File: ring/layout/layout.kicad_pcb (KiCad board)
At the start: 2 copper layers, 58 x 6.2 mm, 62 parts, among them U1 ?, U10 ?, U11 ?, U12 ?, U13 ?, U14 ?, U15 ?, U2 ?, U3 ?, U4 ?, U5 ?, U6 ?, U7 ?, U8 ?, U9 ?, Y1 38.4MHz

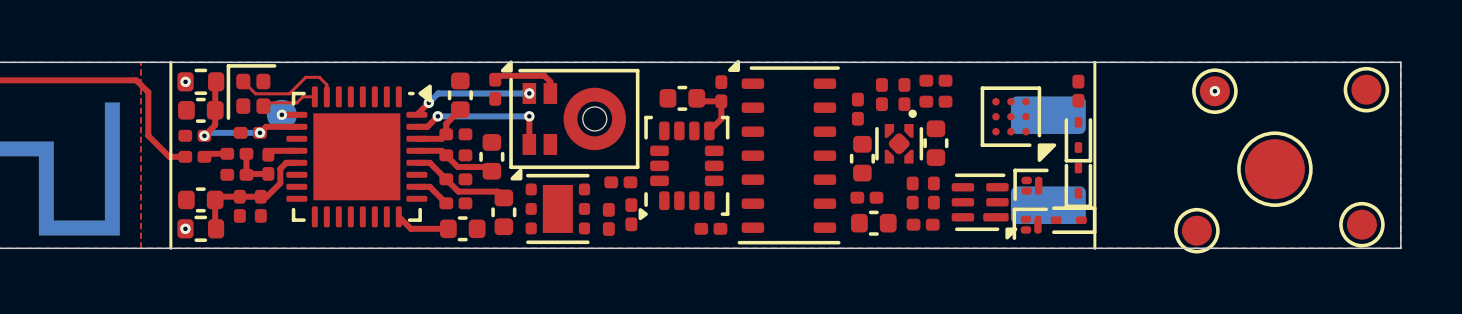
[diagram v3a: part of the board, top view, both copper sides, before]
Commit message: board fully routed; fixing DRC
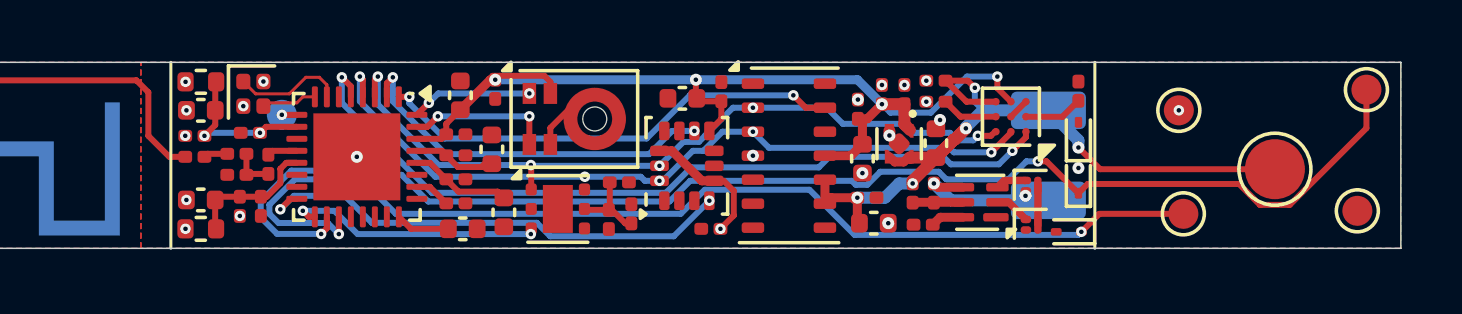
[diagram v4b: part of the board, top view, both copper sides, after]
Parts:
- moved TP6 1.36 mm to (170.6, 81.6)
- moved R2 1.15 mm to (151.9, 84.0), turned to 0 degrees
- moved R1 1.11 mm to (152.3, 85.0), turned to 90 degrees
- moved TP3 0.72 mm to (170.8, 85.0)
- moved TP5 0.49 mm to (176.6, 85.0)
- moved U12 0.39 mm to (166.9, 85.7)
- moved C8 0.25 mm to (147.7, 82.9)
- moved U2 0.16 mm to (166.3, 83.1)
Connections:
- net battery.N59 renamed battery.N61
- net hbt.N152 renamed hbt.N154
- net imu.N232 renamed imu.N234
- net imu.N233 renamed imu.N235
- TP3 pad 1: sda -> swdio
- TP4 pad 1: scl -> swclk
- U12 pad 1: sda -> swdio
- U13 pad 1: scl -> swclk
- U6 pad 1: bat_low -> hbt_int
- U6 pad 14: N381 -> N383
- U6 pad 15: N380 -> N382
- U6 pad 18: N382 -> swclk
- U6 pad 19: N383 -> swdio
- U6 pad 2: hbt_int -> imu_int2
- U6 pad 3: imu_int2 -> scl
- U6 pad 5: scl -> bat_low
- U6 pad 6: N379 -> N381
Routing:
- net swclk: track 0.00 -> 45.2 mm, vias 0 -> 2
- net swdio: track 0.00 -> 36.0 mm, vias 0 -> 2
- net VDD: track 13.8 -> 46.9 mm, vias 2 -> 7
- net bat_low: track 0.00 -> 26.8 mm, vias 0 -> 2
- net VBATT: track 0.00 -> 26.0 mm, vias 0 -> 5
- net sda: track 0.00 -> 25.6 mm, vias 0 -> 5
- net scl: track 0.00 -> 25.3 mm, vias 0 -> 5
- net imu_int1: track 0.00 -> 16.2 mm, vias 0 -> 2
- net hbt_int: track 0.00 -> 15.7 mm, vias 0 -> 2
- net imu_int2: track 0.00 -> 12.6 mm, vias 0 -> 2
- net tmp_int: track 0.00 -> 8.40 mm, vias 0 -> 2
- net battery.bat_vss: track 0.00 -> 5.24 mm, vias 0 -> 2
- net GND: track 0.00 -> 3.35 mm, vias 1 -> 19
- net batman.bin: track 0.00 -> 1.97 mm
- net batman.batman_vdd_out: track 0.00 -> 1.89 mm
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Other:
- rule pad_to_mask_clearance: 0.1 -> 0

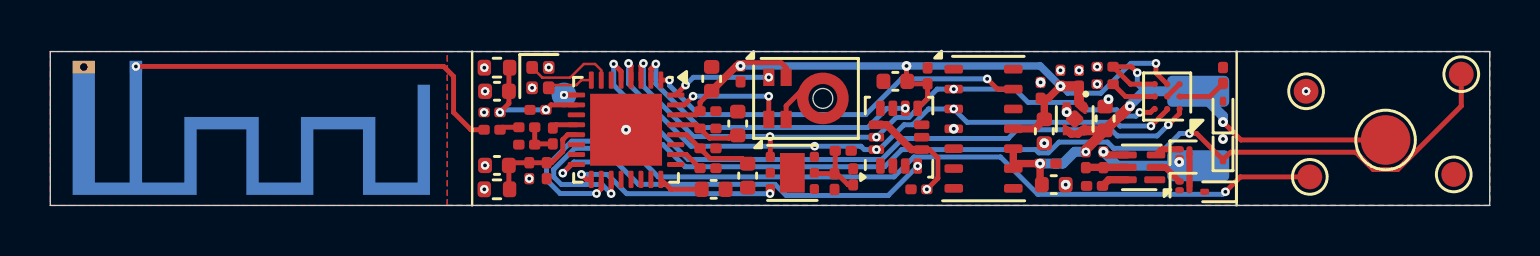
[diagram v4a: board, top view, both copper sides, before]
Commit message: pretty rounded tracks; breaks everything though
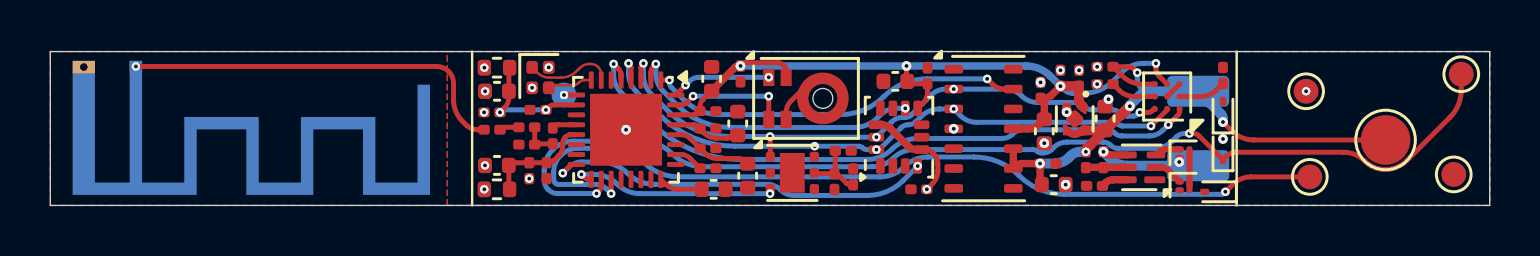
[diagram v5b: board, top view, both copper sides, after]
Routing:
- net VDD: track 46.9 -> 46.0 mm
- net bat_low: track 26.8 -> 26.2 mm
- net VBATT: track 26.0 -> 25.4 mm
- net scl: track 25.3 -> 24.8 mm

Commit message: drc passes
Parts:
- moved TP5 4.26 mm to (180.8, 85.2)
- moved TP6 4.24 mm to (174.8, 81.0)
- moved TP3 4.05 mm to (174.8, 85.2)
- moved TP2 4.02 mm to (177.8, 83.1)
- moved TP4 3.95 mm to (180.8, 81.0)
- moved C6 0.86 mm to (147.3, 83.8)
- moved C8 0.38 mm to (147.7, 82.5)
- moved U4 0.21 mm to (165.7, 85.2)
- moved C5 0.10 mm to (148.1, 85.1)
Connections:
- net N381 renamed NC
- net N382 renamed NC_2
- net N383 renamed NC_3
- net N384 renamed NC_4
- net N385 renamed NC_5
- net N386 renamed NC_6
- net N387 renamed NC_7
- net battery.N61 renamed battery.NC
- net cpu.N520 renamed cpu.NC
- net hbt.N154 renamed hbt.NC
- net imu.N234 renamed imu.NC
- net imu.N235 renamed imu.NC_2
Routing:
- net VDD: track 46.0 -> 77.8 mm, vias 7 -> 10
- net swclk: track 44.8 -> 48.0 mm
- net GND: track 3.30 -> 6.02 mm, vias 19 -> 82
- net swdio: track 35.5 -> 38.1 mm
- net VBATT: track 25.4 -> 27.7 mm
- net scl: track 24.8 -> 26.8 mm
- net sda: track 25.2 -> 26.7 mm
- net imu_int1: track 15.9 -> 14.8 mm
- net mic_data: track 4.02 -> 4.67 mm
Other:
- board size 58 x 6.2 mm -> 62 x 6.2 mm
- board text removed: "we get 6.28 * (dist off finger) extra length!"

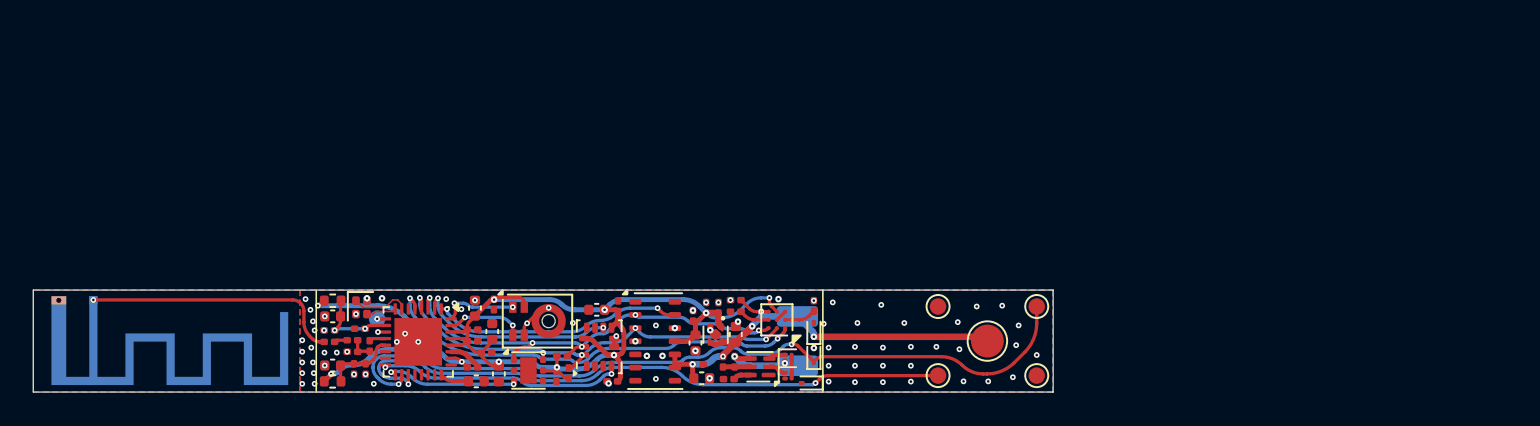
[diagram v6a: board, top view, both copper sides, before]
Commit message: replaced mcu, removed old connections in layout
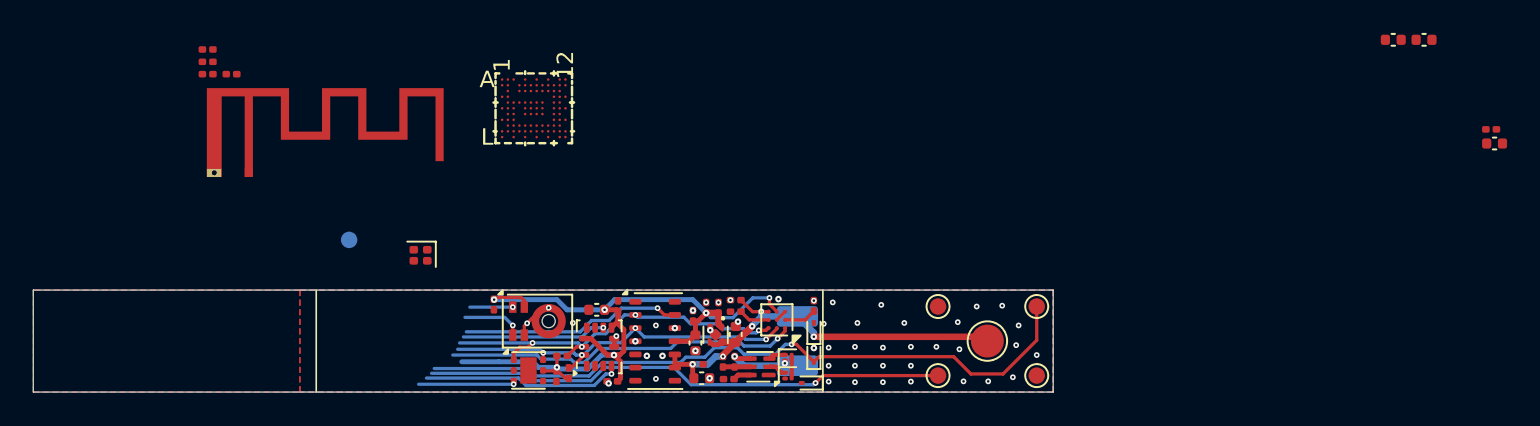
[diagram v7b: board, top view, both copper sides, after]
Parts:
- removed the C10 at (146.7, 81.1)
- removed the C11 at (146.5, 82.4)
- removed the C12 at (139.2, 83.8)
- removed the C13 at (137.8, 83.2)
- removed the C14 at (140.0, 84.8)
- removed the C15 at (139.3, 84.8)
- removed the C16 at (138.0, 84.6)
- removed the C17 at (139.7, 82.3)
- removed the C18 at (137.8, 82.5)
- removed the C19 at (138.0, 81.6)
- removed FB1, FB2: 0 0Hz, R_0402_1005Metric:R_0402_1005Metric
- C5: value 10uF -> 100nF; footprint C_0402_1005Metric:C_0402_1005Metric -> C_0201_0603Metric:C_0201_0603Metric
- C6, C7: value 100nF -> 1uF; footprint C_0201_0603Metric:C_0201_0603Metric -> C_0402_1005Metric:C_0402_1005Metric
- C8: value 1uF -> 1.6pF; footprint C_0402_1005Metric:C_0402_1005Metric -> C_0201_0603Metric:C_0201_0603Metric
- C9: value 10nF -> 18pF
- L2: value 3.2nH -> 3.200000000000001nH
- U6: footprint QFN-32-1EP_4x4mm_P0.4mm_EP2.9x2.9mm:QFN-32-1EP_4x4mm_P0.4mm_EP2.9x2.9mm -> WLCSP95_4.390X3.994_NOR:WLCSP95_4.390X3.994_NOR
- U7: moved to F.Cu
- Y1: value 38.4MHz -> 32MHz; footprint Crystal_SMD_1210-4Pin_1.2x1.0mm:Crystal_SMD_1210-4Pin_1.2x1.0mm -> Crystal_SMD_2016-4Pin_2.0x1.6mm:Crystal_SMD_2016-4Pin_2.0x1.6mm
- moved C6 62.6 mm to (208.6, 71.1)
- moved C5 62.1 mm to (208.4, 70.2), turned to 0 degrees
- moved C7 61.2 mm to (204.3, 64.8)
- moved C4 59.5 mm to (202.5, 64.8)
- moved C9 23.4 mm to (130.4, 66.1)
- moved C8 23.3 mm to (130.4, 66.9), turned to 0 degrees
- moved L2 19.7 mm to (130.4, 65.4), turned to 0 degrees
- moved L1 18.5 mm to (131.8, 66.9), turned to 0 degrees
- moved U6 15.8 mm to (150.2, 69.0), turned to 0 degrees
- moved U7 12.2 mm to (132.9, 72.9)
- moved TP1 5.09 mm to (139.0, 77.0)
- moved Y1 4.79 mm to (143.3, 77.9), turned to -90 degrees
- renumbered C20 to C10, C21 to C11, C22 to C12, C23 to C13, C24 to C14, C25 to C15, C26 to C16, C27 to C17, C28 to C18, C29 to C19, C30 to C20, C31 to C21
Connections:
- C4 pad 1: cpu.decouple -> cpu.decusb
- C8 pad 1: VDD -> cpu.ant_match.out1
- C9 pad 1: VDD -> cpu.ant_match.out2
- C9 pad 2: GND -> cpu.ant_match.out3
- L1 pad 1: cpu.ant -> NC_6
- L1 pad 2: cpu.ant.out1 -> cpu.ant_match.out1
- L2 pad 1: cpu.ant.out1 -> cpu.ant_match.out1
- L2 pad 2: cpu.ant.out2 -> cpu.ant_match.out2
- U7 pad 1: cpu.ant.out3 -> cpu.ant_match.out3
- Y1 pad 1: cpu.xin -> cpu.xc1
- Y1 pad 3: cpu.xout -> cpu.xc2
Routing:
- net VDD: track 77.8 -> 48.7 mm, vias 10 -> 6
- net cpu.ant.out3: track 15.8 -> 0.00 mm, vias 1 -> 0
- net swclk: track 48.0 -> 41.8 mm, vias 2 -> 1
- net swdio: track 38.1 -> 32.0 mm, vias 2 -> 1
- net cpu.rfvdd: track 5.11 -> 0.00 mm, vias 2 -> 0
- net bat_low: track 26.3 -> 21.6 mm, vias 2 -> 1
- net cpu.pavdd: track 4.40 -> 0.00 mm
- net sda: track 26.7 -> 22.4 mm, vias 5 -> 4
- net cpu.xin: track 3.77 -> 0.00 mm
- net scl: track 26.8 -> 23.2 mm, vias 5 -> 4
- net imu_int2: track 12.2 -> 8.73 mm, vias 2 -> 1
- net imu_int1: track 14.8 -> 12.2 mm, vias 2 -> 1
- net tmp_int: track 7.98 -> 5.78 mm, vias 2 -> 1
- net mic_data: track 4.67 -> 2.61 mm, vias 2 -> 1
- net GND: track 6.02 -> 4.06 mm, vias 82 -> 50
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
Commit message: nrf laid out but unrouted; probably have to switch for manufacturing
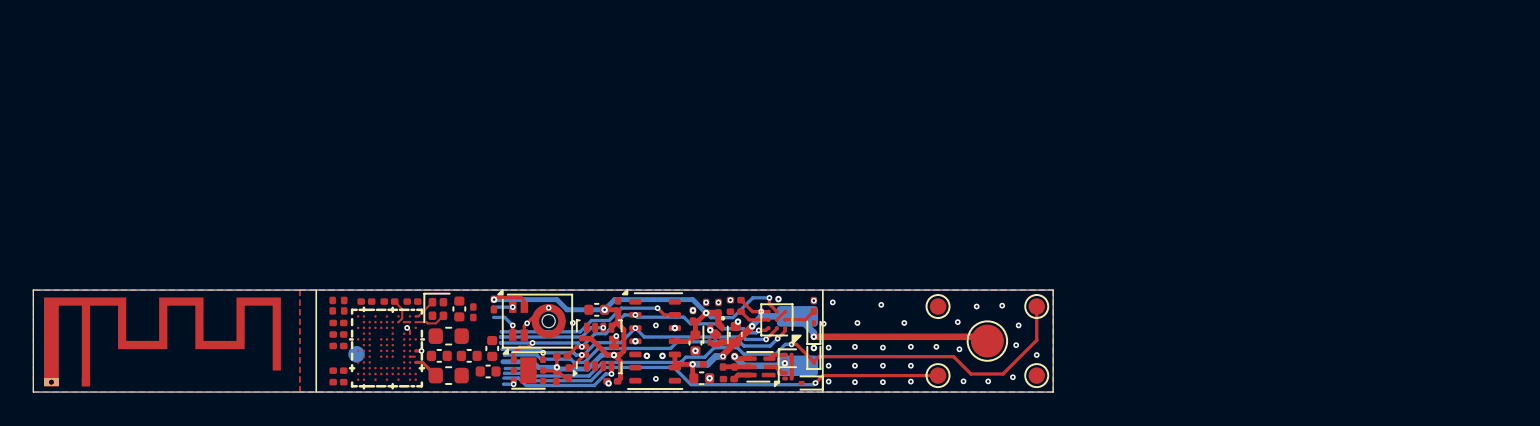
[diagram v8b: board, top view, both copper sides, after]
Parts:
- added C10: 100nF, C_0201_0603Metric:C_0201_0603Metric, F.Cu at (140.1, 80.7)
- added C11: 1uF, C_0402_1005Metric:C_0402_1005Metric, F.Cu at (146.3, 84.0)
- added C12: 1uF, C_0402_1005Metric:C_0402_1005Metric, F.Cu at (144.5, 84.0)
- added C13: 1uF, C_0402_1005Metric:C_0402_1005Metric, F.Cu at (147.7, 83.5)
- added C14: 1uF, C_0402_1005Metric:C_0402_1005Metric, F.Cu at (147.4, 85.0)
- added C15: 1uF, C_0402_1005Metric:C_0402_1005Metric, F.Cu at (145.7, 81.2)
- added C16: 2.2nF, C_0201_0603Metric:C_0201_0603Metric, F.Cu at (146.6, 81.3)
- added C17: 700fF, C_0201_0603Metric:C_0201_0603Metric, F.Cu at (138.0, 81.0)
- added L3: 2.2nH, L_0201_0603Metric:L_0201_0603Metric, F.Cu at (138.7, 81.0)
- added L4: 2.2nH, L_0201_0603Metric:L_0201_0603Metric, F.Cu at (138.3, 82.0)
- C4, C6, C7: value 1uF -> 100nF; footprint C_0402_1005Metric:C_0402_1005Metric -> C_0201_0603Metric:C_0201_0603Metric
- C8: value 1.6pF -> 100nF
- C9: value 18pF -> 100nF
- L1: value 2nH -> 10uH; footprint L_0201_0603Metric:L_0201_0603Metric -> L_0603_1608Metric:L_0603_1608Metric
- L2: value 3.200000000000001nH -> 10uH; footprint L_0201_0603Metric:L_0201_0603Metric -> L_0603_1608Metric:L_0603_1608Metric
- moved C6 71.8 mm to (138.3, 85.6), turned to 180 degrees
- moved C7 68.6 mm to (138.3, 83.4), turned to 180 degrees
- moved C5 67.8 mm to (141.4, 80.7), turned to 180 degrees
- moved C4 61.7 mm to (142.8, 80.7), turned to 180 degrees
- moved L2 22.8 mm to (145.1, 82.8)
- moved L1 22.6 mm to (145.1, 85.2)
- moved C9 20.4 mm to (138.3, 84.9), turned to 180 degrees
- moved C8 17.7 mm to (138.3, 82.7), turned to 180 degrees
- moved U6 17.1 mm to (141.3, 83.5), turned to -90 degrees
- moved U7 16.1 mm to (123.0, 85.6)
- moved TP1 6.96 mm to (139.4, 83.9)
- moved Y1 3.43 mm to (144.4, 81.2), turned to 0 degrees
- renumbered C10 to C18, C11 to C19, C12 to C20, C13 to C21, C14 to C22, C15 to C23, C16 to C24, C17 to C25, C18 to C26, C19 to C27, C20 to C28, C21 to C29
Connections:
- net cpu.dcch renamed cpu.NC_6
- net cpu.xl1 renamed cpu.NC
- net cpu.xl2 renamed cpu.NC_2
- C4 pad 1: cpu.decusb -> VDD
- C8 pad 1: cpu.ant_match.out1 -> VDD
- C9 pad 1: cpu.ant_match.out2 -> VDD
- C9 pad 2: cpu.ant_match.out3 -> GND
- L1 pad 1: NC_6 -> cpu.dccd
- L1 pad 2: cpu.ant_match.out1 -> cpu.decd
- L2 pad 1: cpu.ant_match.out1 -> cpu.dcc
- L2 pad 2: cpu.ant_match.out2 -> cpu.decr
- TP4 pad 1: swclk -> swdclk
- U13 pad 1: swclk -> swdclk
- U6 pad A11: NC_5 -> cpu.NC_4
- U6 pad A12: NC_4 -> cpu.NC_3
- U6 pad A5: (no net) -> GND
- U6 pad A9: (no net) -> cpu.dccd
- U6 pad B1: cpu.decrf -> cpu.decr
- U6 pad B11: VDD -> GND
- U6 pad C10: NC_54 -> NC_37
- U6 pad C11: cpu.decusb -> cpu.NC_5
- U6 pad C4: NC_37 -> NC_22
- U6 pad C5: NC_38 -> NC_23
- U6 pad C6: NC_50 -> NC_33
- U6 pad C7: NC_51 -> NC_34
- U6 pad C8: NC_52 -> NC_35
- U6 pad C9: NC_53 -> NC_36
- U6 pad D1: NC_6 -> cpu.ant
- U6 pad D10: NC_39 -> NC_24
- U6 pad E10: NC_40 -> NC_25
- U6 pad E2: NC_36 -> NC_21
- U6 pad E3: NC_35 -> NC_20
- U6 pad E4: NC_49 -> NC_32
- U6 pad F1: NC_2 -> swdio
- U6 pad F10: NC_12 -> NC_4
- U6 pad F2: NC -> swdclk
- U6 pad F3: NC_47 -> NC_30
- U6 pad G10: NC_11 -> NC_3
- U6 pad G11: NC_9 -> NC
- U6 pad G2: NC_3 -> rst
- U6 pad G3: NC_46 -> NC_29
- U6 pad H1: NC_34 -> NC_19
- U6 pad H10: NC_13 -> NC_5
- U6 pad H12: NC_10 -> NC_2
- U6 pad H2: NC_48 -> NC_31
- U6 pad H3: NC_30 -> hbt_int
- U6 pad J10: NC_14 -> NC_6
- U6 pad J11: NC_41 -> sda
- U6 pad J2: NC_33 -> NC_18
- U6 pad J3: NC_45 -> NC_28
- U6 pad J4: NC_28 -> bat_low
- U6 pad J5: NC_26 -> imu_int1
- U6 pad J6: NC_19 -> NC_11
- U6 pad J7: NC_18 -> NC_10
- U6 pad J8: NC_17 -> NC_9
- U6 pad J9: NC_16 -> NC_8
- U6 pad K10: NC_20 -> NC_12
- U6 pad K12: NC_42 -> scl
- U6 pad K2: NC_31 -> mic_clk
- U6 pad K3: NC_43 -> NC_26
- U6 pad K4: NC_29 -> tmp_int
- U6 pad K5: NC_27 -> imu_int2
- U6 pad K7: NC_25 -> NC_17
- U6 pad K8: NC_23 -> NC_15
- U6 pad K9: NC_21 -> NC_13
- U6 pad L1: NC_32 -> mic_data
- U6 pad L12: NC_15 -> NC_7
- U6 pad L3: NC_44 -> NC_27
- U6 pad L7: NC_24 -> NC_16
- U6 pad L9: NC_22 -> NC_14
- U7 pad 1: cpu.ant_match.out3 -> cpu.antenna.n2
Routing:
- net swclk: track 41.8 -> 0.00 mm, vias 1 -> 0
- net swdclk: track 0.00 -> 37.5 mm, vias 0 -> 1
- net tmp_int: track 5.78 -> 0.60 mm
- net imu_int1: track 12.2 -> 7.51 mm
- net swdio: track 32.0 -> 27.5 mm
- net bat_low: track 21.6 -> 18.4 mm
- net sda: track 22.4 -> 19.7 mm
- net scl: track 23.2 -> 20.7 mm
- net imu_int2: track 8.73 -> 6.48 mm
- net hbt_int: track 13.4 -> 11.3 mm
- net cpu.xc2: track 0.00 -> 1.91 mm
- net mic_clk: track 3.70 -> 1.94 mm
- net cpu.dccd: track 0.00 -> 1.54 mm
- net mic_data: track 2.61 -> 1.20 mm
- net cpu.xc1: track 0.00 -> 1.37 mm
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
